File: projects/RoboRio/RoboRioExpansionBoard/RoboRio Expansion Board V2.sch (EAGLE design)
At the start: 84 parts, among them J1 RRINTERFACE-FEMALE, J2 MICROSD, Q1 5.0 MHz, T1 NPN-SOT416, U1 P8X32A-Q44, U2 24LC256ST, U3 FT232RFTR232R, U4 MC1525TO, U6 RT9193-33GB

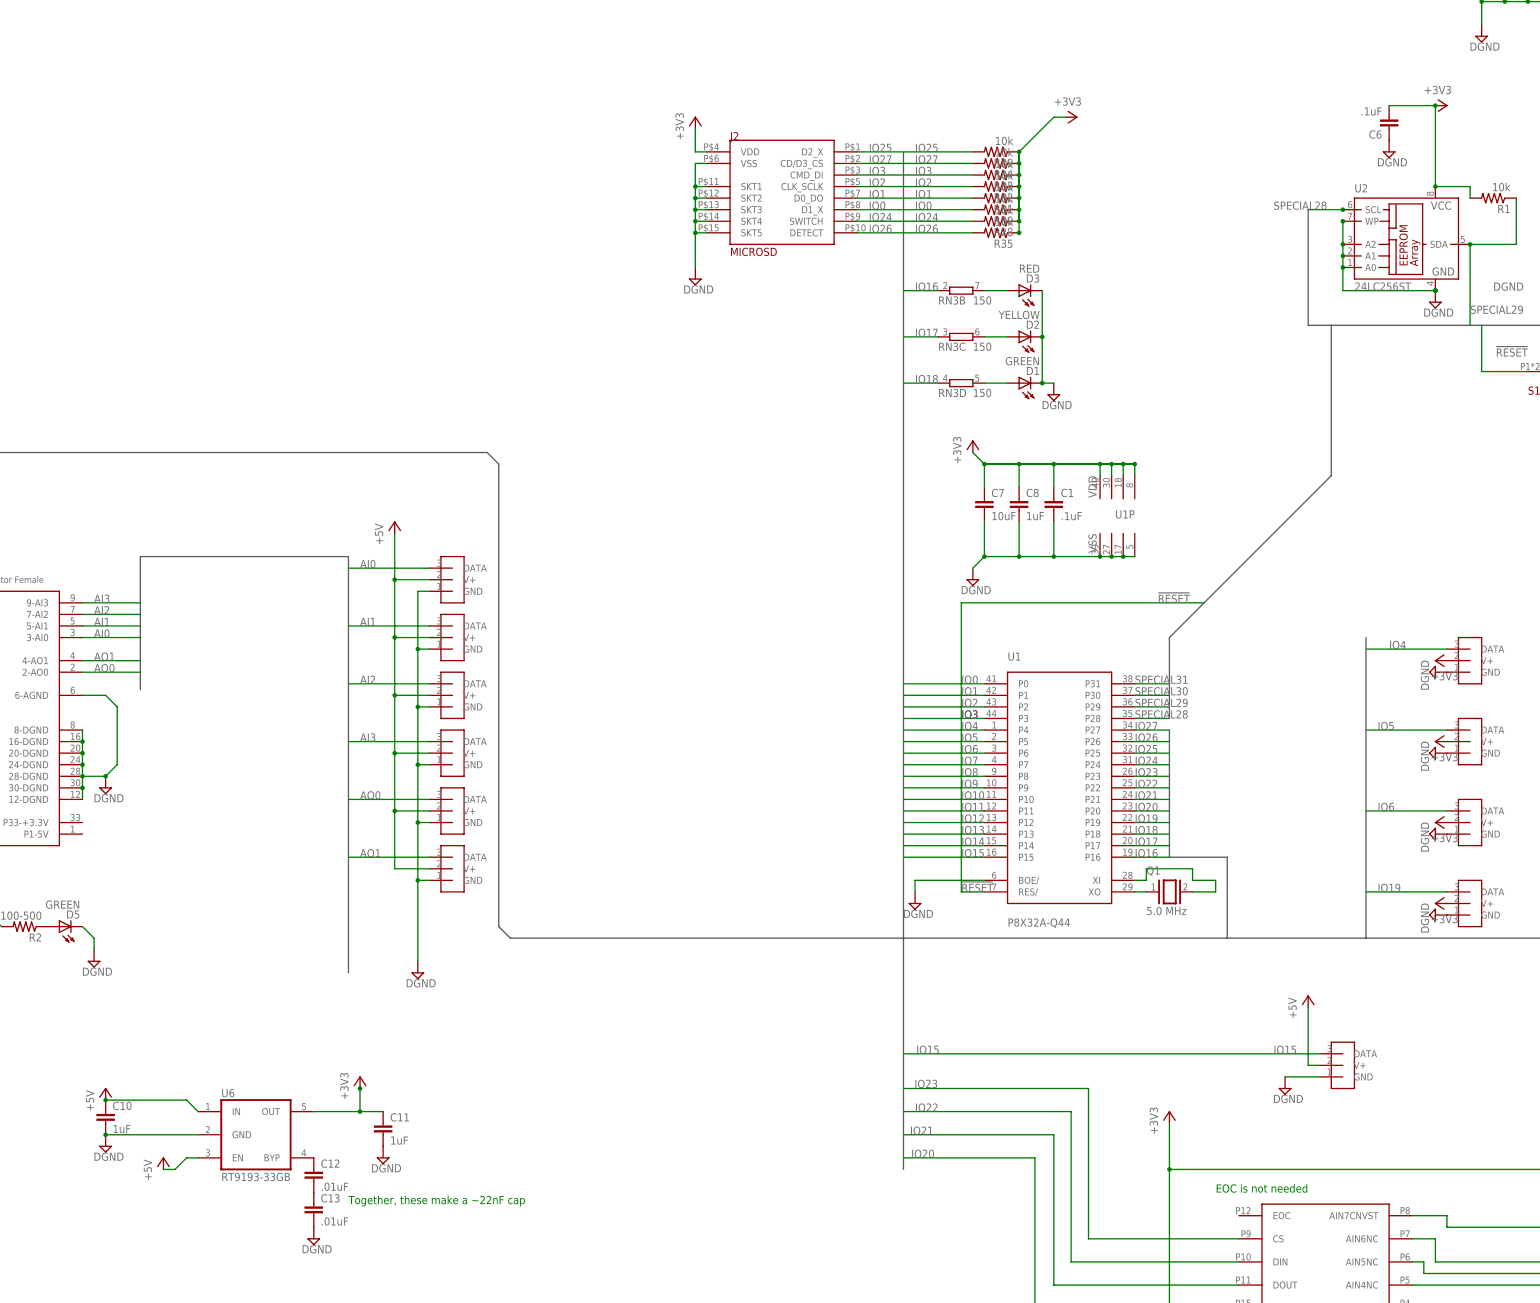
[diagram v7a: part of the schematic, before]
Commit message: Added 2x 3.3v regs
Apparently we are using that package.
5v is still not connected, we need to do a ltspice simulation on our
current design idea before putting it here.
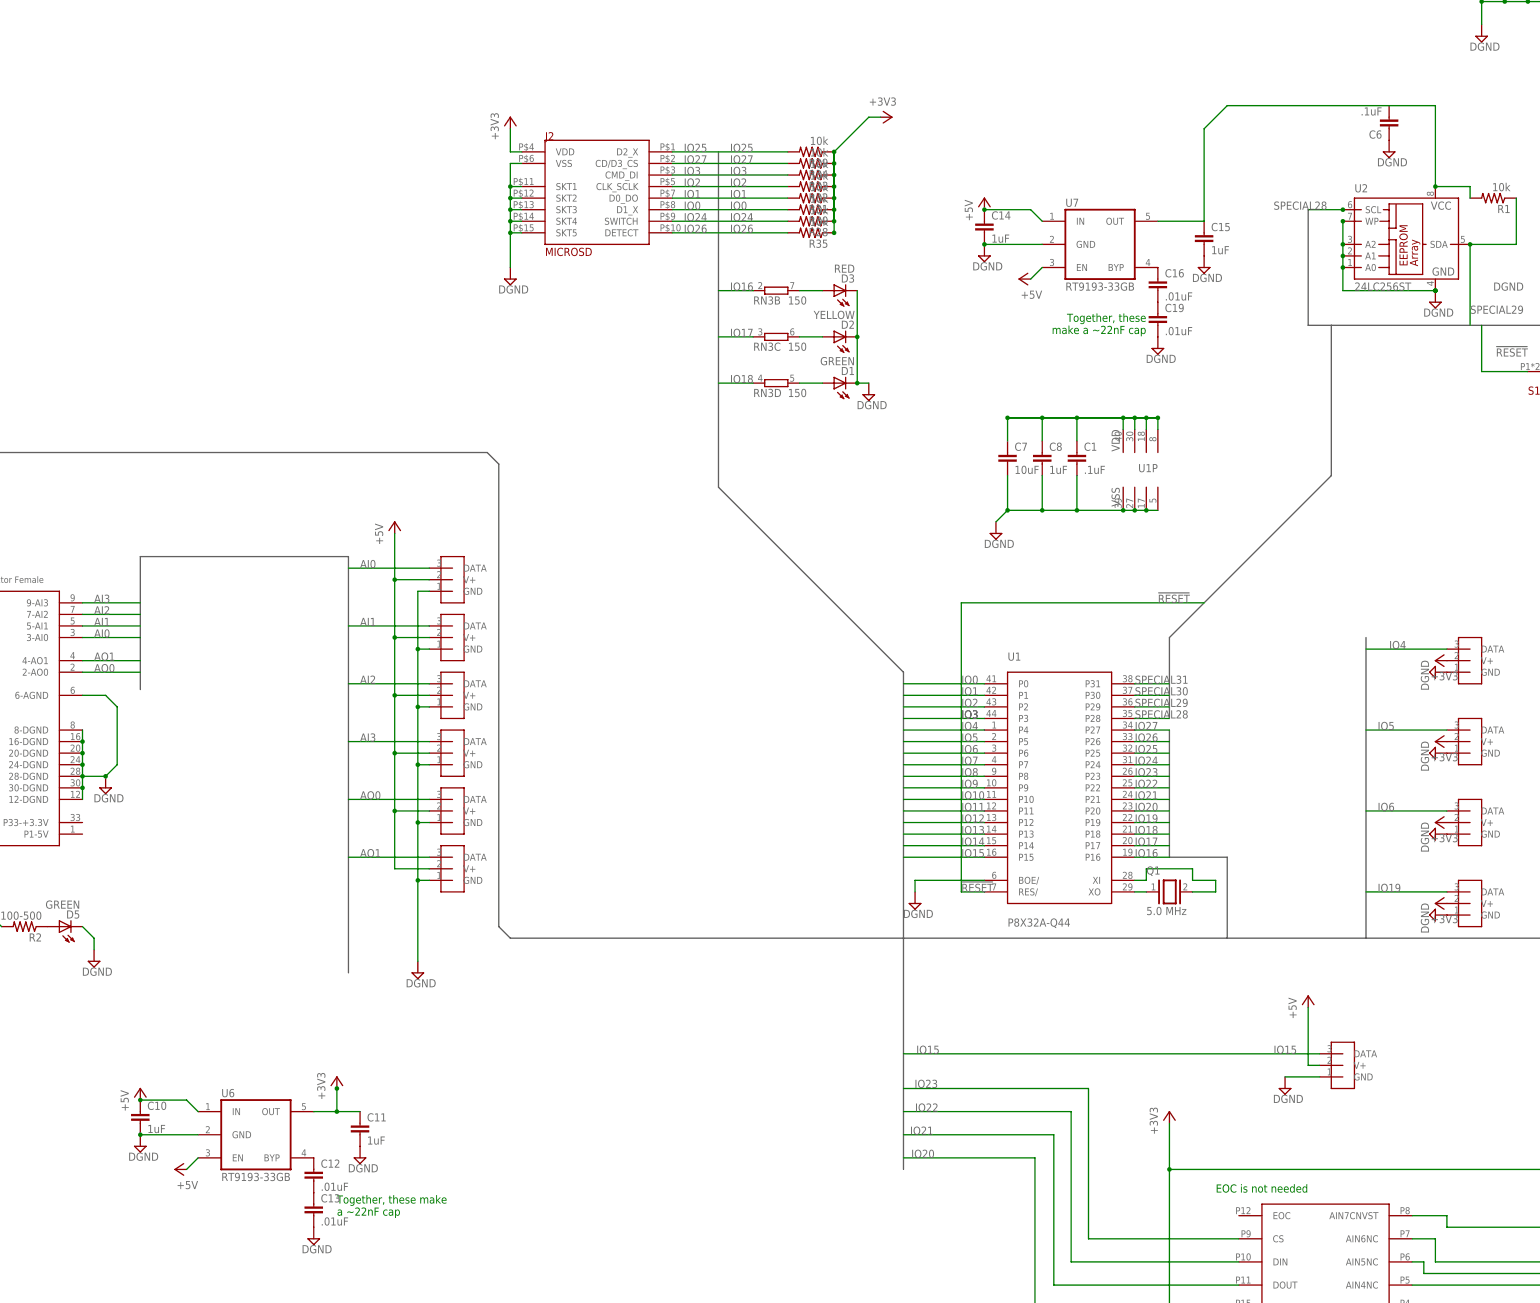
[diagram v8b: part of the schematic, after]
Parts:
- added C14, C15: 1uF, resistor:C-EUC0603K
- added C16, C19: .01uF, resistor:C-EUC0603K
- added U7: RT9193-33GB, dp_devices:VREG_5PINS-SOT-23-5
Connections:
- new net +3V3_PROP: C15.1, C6.2, R1.2, U2.VCC, U7.OUT
- new net N$15: C16.2, C19.1
- new net N$20: C16.1, U7.BYP
- new net N$21: C1.1, C7.1, C8.1, U1P.VDD@1, U1P.VDD@2, U1P.VDD@3, U1P.VDD@4
- net +3V3: no longer C1.1, C6.2, C7.1, C8.1, R1.2, U1P.VDD@1, U1P.VDD@2, U1P.VDD@3, U1P.VDD@4, U2.VCC
- net +5V: now also C14.1, U7.EN, U7.IN
- net DGND: now also C14.2, C15.2, C19.2, U7.GND
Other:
- moved on the sheet: C1, C10, C11, C7, C8, D1, D2, D3, J2, R28, R29, R30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
